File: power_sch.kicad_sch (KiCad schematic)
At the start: 18 parts, among them Q6 RUM002N05T2L, Q7 RUM002N05T2L, U3 TPS7A2601DRVR, U4 TPS7A2601DRVR

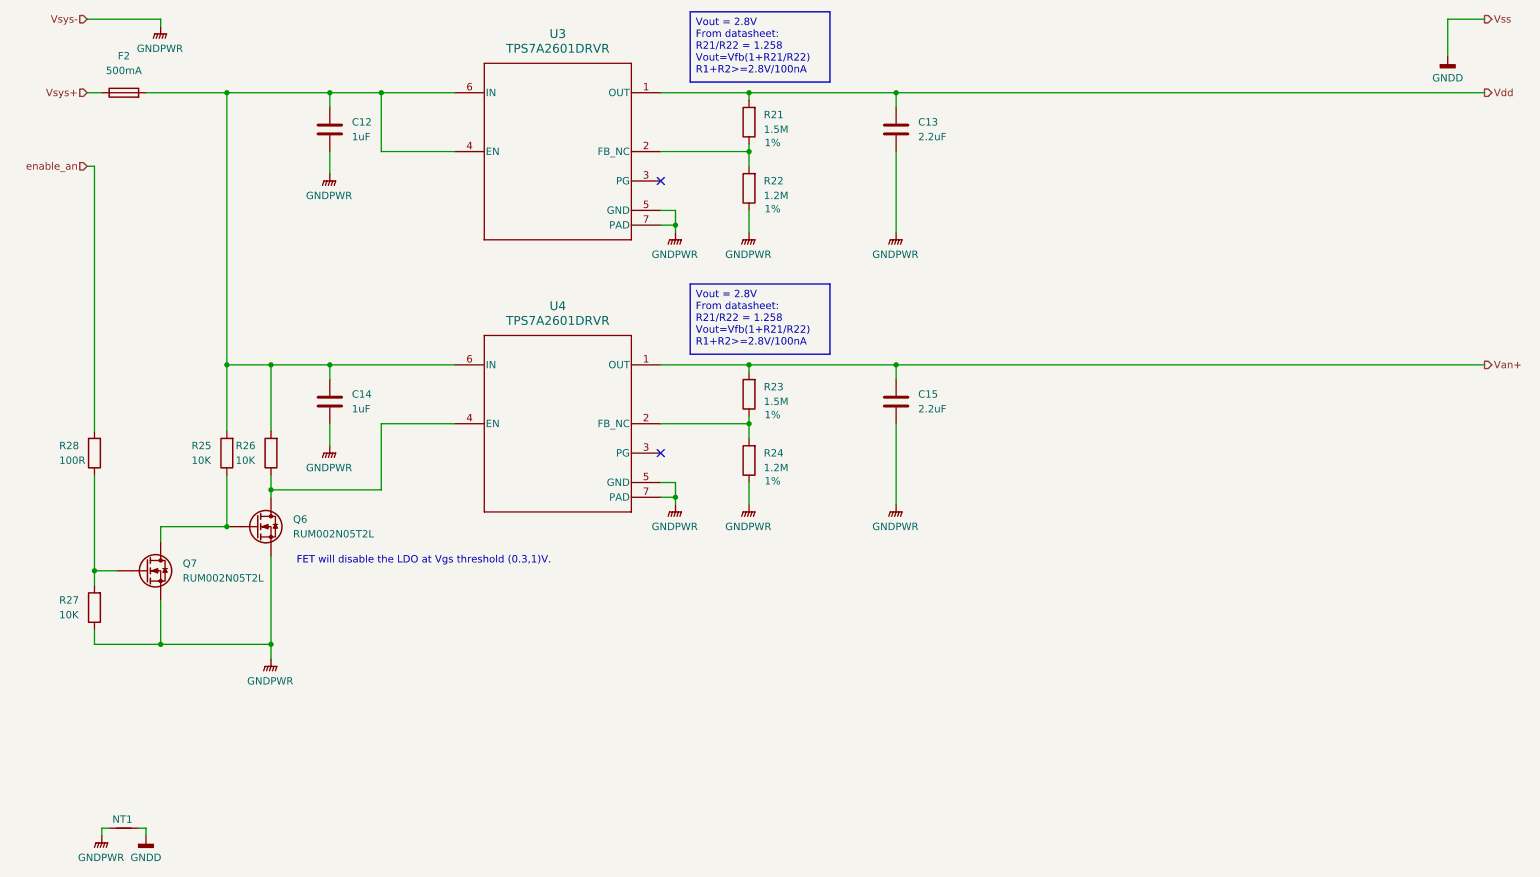
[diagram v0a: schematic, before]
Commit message: Add wiring, change footprint to avoid fatal errors at pads.
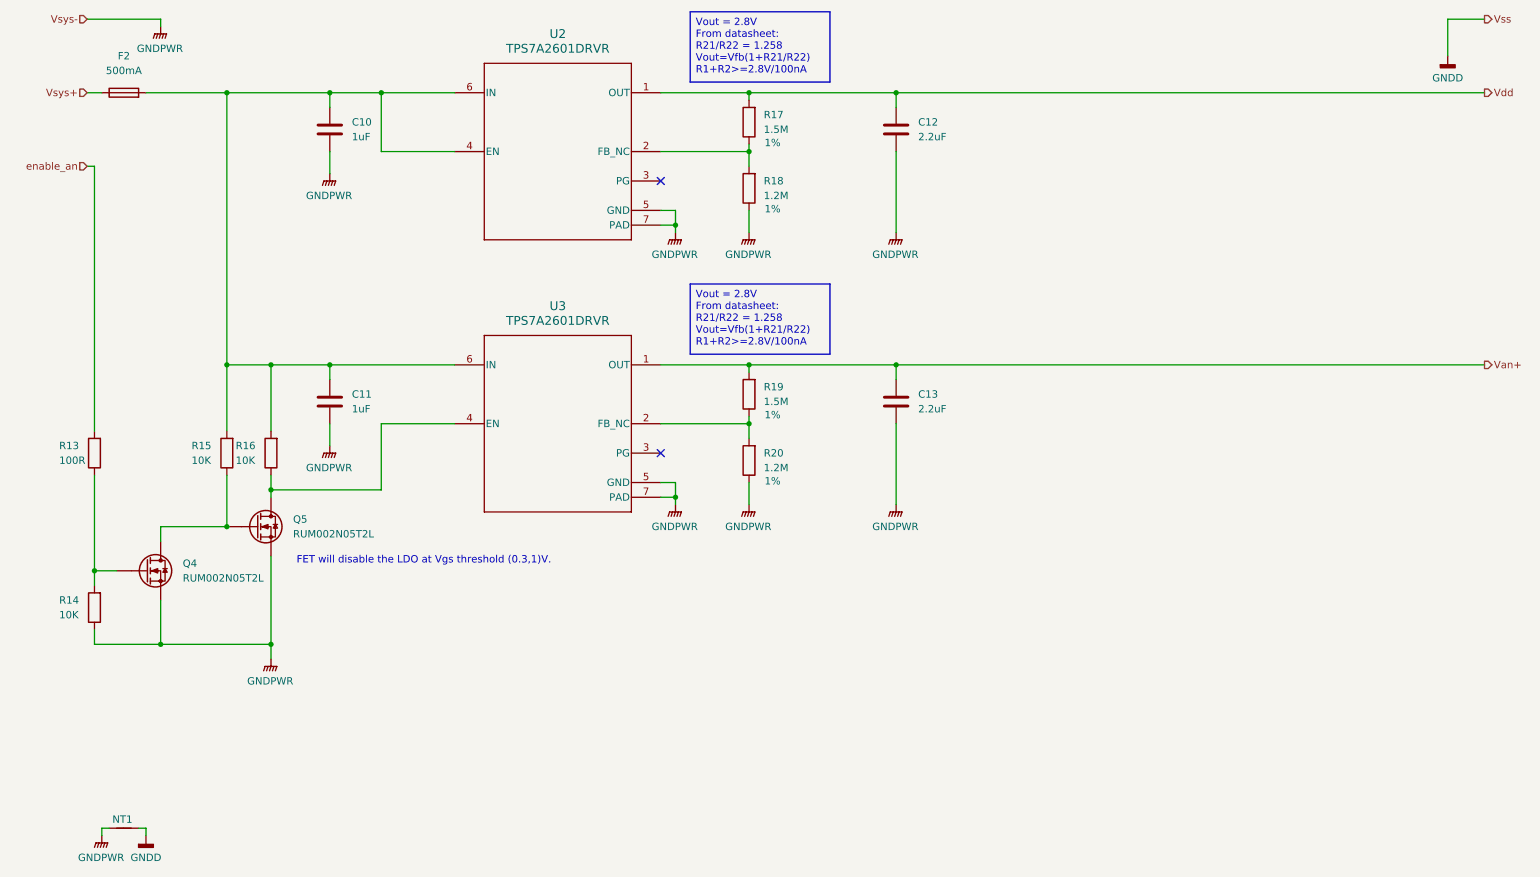
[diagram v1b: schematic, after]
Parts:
- renumbered C12 to C10, C14 to C11, C13 to C12, C15 to C13, Q7 to Q4, Q6 to Q5, R28 to R13, R27 to R14, R25 to R15, R26 to R16, R21 to R17, R22 to R18, R23 to R19, R24 to R20, U3 to U2, U4 to U3
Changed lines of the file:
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@@
 		(dnp no)
 		(fields_autoplaced yes)
-		(property "Reference" "C13"
+		(property "Reference" "C12"
 			(at 168.91 49.5299 0)
 			(show_name no)
@@
 			(project "MoistureESP"
 				(path "/f2b9f638-139e-46ec-aa60-77c4af989196/49685a81-7509-4241-9c59-8f2ca08912fe"
-					(reference "C13")
+					(reference "C12")
 					(unit 1)
 				)
@@
 		(in_pos_files yes)
 		(dnp no)
-		(property "Reference" "R24"
+		(property "Reference" "R20"
 			(at 142.24 106.6799 0)
 			(show_name no)
@@
 			(project "MoistureESP"
 				(path "/f2b9f638-139e-46ec-aa60-77c4af989196/49685a81-7509-4241-9c59-8f2ca08912fe"
-					(reference "R24")
+					(reference "R20")
 					(unit 1)
 				)
@@
 		(in_pos_files yes)
 		(dnp no)
-		(property "Reference" "R23"
+		(property "Reference" "R19"
 			(at 142.24 95.2499 0)
 			(show_name no)
@@
 			(project "MoistureESP"
 				(path "/f2b9f638-139e-46ec-aa60-77c4af989196/49685a81-7509-4241-9c59-8f2ca08912fe"
-					(reference "R23")
+					(reference "R19")
 					(unit 1)
 				)
@@
 		(dnp no)
 		(fields_autoplaced yes)
-		(property "Reference" "#PWR061"
+		(property "Reference" "#PWR031"
 			(at 67.31 63.5 0)
 			(hide yes)
@@
 			(project "MoistureESP"
 				(path "/f2b9f638-139e-46ec-aa60-77c4af989196/49685a81-7509-4241-9c59-8f2ca08912fe"
-					(reference "#PWR061")
+					(reference "#PWR031")
 					(unit 1)
 				)
@@
 		(dnp no)
 		(fields_autoplaced yes)
-		(property "Reference" "#PWR09"
+		(property "Reference" "#PWR028"
 			(at 35.56 179.07 0)
 			(hide yes)
@@
 			(project "MoistureESP"
 				(path "/f2b9f638-139e-46ec-aa60-77c4af989196/49685a81-7509-4241-9c59-8f2ca08912fe"
-					(reference "#PWR09")
+					(reference "#PWR028")
 					(unit 1)
 				)
@@
 		(in_pos_files yes)
 		(dnp no)
-		(property "Reference" "R25"
+		(property "Reference" "R15"
 			(at 43.434 105.41 0)
 			(show_name no)
@@
 			(project "MoistureESP"
 				(path "/f2b9f638-139e-46ec-aa60-77c4af989196/49685a81-7509-4241-9c59-8f2ca08912fe"
-					(reference "R25")
+					(reference "R15")
 					(unit 1)
 				)
@@
 		(dnp no)
 		(fields_autoplaced yes)
-		(property "Reference" "#PWR073"
+		(property "Reference" "#PWR034"
 			(at 127 120.65 0)
 			(hide yes)
@@
 			(project "MoistureESP"
 				(path "/f2b9f638-139e-46ec-aa60-77c4af989196/49685a81-7509-4241-9c59-8f2ca08912fe"
-					(reference "#PWR073")
+					(reference "#PWR034")
 					(unit 1)
 				)
@@
 		(dnp no)
 		(fields_autoplaced yes)
-		(property "Reference" "U3"
+		(property "Reference" "U2"
 			(at 106.68 34.29 0)
 			(show_name no)
@@
 			(project "MoistureESP"
 				(path "/f2b9f638-139e-46ec-aa60-77c4af989196/49685a81-7509-4241-9c59-8f2ca08912fe"
-					(reference "U3")
+					(reference "U2")
 					(unit 1)
 				)
@@
 		(dnp no)
 		(fields_autoplaced yes)
-		(property "Reference" "#PWR068"
+		(property "Reference" "#PWR033"
 			(at 127 73.66 0)
 			(hide yes)
@@
 			(project "MoistureESP"
 				(path "/f2b9f638-139e-46ec-aa60-77c4af989196/49685a81-7509-4241-9c59-8f2ca08912fe"
-					(reference "#PWR068")
+					(reference "#PWR033")
 					(unit 1)
 				)
@@
 		(dnp no)
 		(fields_autoplaced yes)
-		(property "Reference" "#PWR018"
+		(property "Reference" "#PWR039"
 			(at 260.35 44.45 0)
 			(hide yes)
@@
 			(project "MoistureESP"
 				(path "/f2b9f638-139e-46ec-aa60-77c4af989196/49685a81-7509-4241-9c59-8f2ca08912fe"
-					(reference "#PWR018")
+					(reference "#PWR039")
 					(unit 1)
 				)
@@
 		(dnp no)
 		(fields_autoplaced yes)
-		(property "Reference" "#PWR076"
+		(property "Reference" "#PWR032"
 			(at 67.31 110.49 0)
 			(hide yes)
@@
 			(project "MoistureESP"
 				(path "/f2b9f638-139e-46ec-aa60-77c4af989196/49685a81-7509-4241-9c59-8f2ca08912fe"
-					(reference "#PWR076")
+					(reference "#PWR032")
 					(unit 1)
 				)
@@
 		(in_pos_files yes)
 		(dnp no)
-		(property "Reference" "R21"
+		(property "Reference" "R17"
 			(at 142.24 48.2599 0)
 			(show_name no)
@@
 			(project "MoistureESP"
 				(path "/f2b9f638-139e-46ec-aa60-77c4af989196/49685a81-7509-4241-9c59-8f2ca08912fe"
-					(reference "R21")
+					(reference "R17")
 					(unit 1)
 				)
@@
 		(dnp no)
 		(fields_autoplaced yes)
-		(property "Reference" "Q6"
+		(property "Reference" "Q5"
 			(at 60.96 118.1099 0)
 			(show_name no)
@@
 			(project "MoistureESP"
 				(path "/f2b9f638-139e-46ec-aa60-77c4af989196/49685a81-7509-4241-9c59-8f2ca08912fe"
-					(reference "Q6")
+					(reference "Q5")
 					(unit 1)
 				)
@@
 		(dnp no)
 		(fields_autoplaced yes)
-		(property "Reference" "C14"
+		(property "Reference" "C11"
 			(at 71.12 96.5199 0)
 			(show_name no)
@@
 			(project "MoistureESP"
 				(path "/f2b9f638-139e-46ec-aa60-77c4af989196/49685a81-7509-4241-9c59-8f2ca08912fe"
-					(reference "C14")
+					(reference "C11")
 					(unit 1)
 				)
@@
 		(dnp no)
 		(fields_autoplaced yes)
-		(property "Reference" "Q7"
+		(property "Reference" "Q4"
 			(at 41.91 125.7299 0)
 			(show_name no)
@@
 			(project "MoistureESP"
 				(path "/f2b9f638-139e-46ec-aa60-77c4af989196/49685a81-7509-4241-9c59-8f2ca08912fe"
-					(reference "Q7")
+					(reference "Q4")
 					(unit 1)
 				)
@@
 		(dnp no)
 		(fields_autoplaced yes)
-		(property "Reference" "#PWR077"
+		(property "Reference" "#PWR030"
 			(at 57.15 147.32 0)
 			(hide yes)
@@
 			(project "MoistureESP"
 				(path "/f2b9f638-139e-46ec-aa60-77c4af989196/49685a81-7509-4241-9c59-8f2ca08912fe"
-					(reference "#PWR077")
+					(reference "#PWR030")
 					(unit 1)
 				)
@@
 		(dnp no)
 		(fields_autoplaced yes)
-		(property "Reference" "#PWR074"
+		(property "Reference" "#PWR036"
 			(at 139.7 120.65 0)
 			(hide yes)
@@
 			(project "MoistureESP"
 				(path "/f2b9f638-139e-46ec-aa60-77c4af989196/49685a81-7509-4241-9c59-8f2ca08912fe"
-					(reference "#PWR074")
+					(reference "#PWR036")
 					(unit 1)
 				)
@@
 		(dnp no)
 		(fields_autoplaced yes)
-		(property "Reference" "#PWR08"
+		(property "Reference" "#PWR027"
 			(at 27.94 177.8 0)
 			(hide yes)
@@
 			(project "MoistureESP"
 				(path "/f2b9f638-139e-46ec-aa60-77c4af989196/49685a81-7509-4241-9c59-8f2ca08912fe"
-					(reference "#PWR08")
+					(reference "#PWR027")
 					(unit 1)
 				)
@@
 		(dnp no)
 		(fields_autoplaced yes)
-		(property "Reference" "C12"
+		(property "Reference" "C10"
 			(at 71.12 49.5299 0)
 			(show_name no)
@@
 			(project "MoistureESP"
 				(path "/f2b9f638-139e-46ec-aa60-77c4af989196/49685a81-7509-4241-9c59-8f2ca08912fe"
-					(reference "C12")
+					(reference "C10")
 					(unit 1)
 				)
@@
 		(in_pos_files yes)
 		(dnp no)
-		(property "Reference" "R22"
+		(property "Reference" "R18"
 			(at 142.24 59.6899 0)
 			(show_name no)
@@
 			(project "MoistureESP"
 				(path "/f2b9f638-139e-46ec-aa60-77c4af989196/49685a81-7509-4241-9c59-8f2ca08912fe"
-					(reference "R22")
+					(reference "R18")
 					(unit 1)
 				)
@@
 		(in_pos_files yes)
 		(dnp no)
-		(property "Reference" "R28"
+		(property "Reference" "R13"
 			(at 20.574 105.41 0)
 			(show_name no)
@@
 			(project "MoistureESP"
 				(path "/f2b9f638-139e-46ec-aa60-77c4af989196/49685a81-7509-4241-9c59-8f2ca08912fe"
-					(reference "R28")
+					(reference "R13")
 					(unit 1)
 				)
@@
 		(in_pos_files yes)
 		(dnp no)
-		(property "Reference" "R27"
+		(property "Reference" "R14"
 			(at 20.574 132.08 0)
 			(show_name no)
@@
 			(project "MoistureESP"
 				(path "/f2b9f638-139e-46ec-aa60-77c4af989196/49685a81-7509-4241-9c59-8f2ca08912fe"
-					(reference "R27")
+					(reference "R14")
 					(unit 1)
 				)
@@
 		(dnp no)
 		(fields_autoplaced yes)
-		(property "Reference" "C15"
+		(property "Reference" "C13"
 			(at 168.91 96.5199 0)
 			(show_name no)
@@
 			(project "MoistureESP"
 				(path "/f2b9f638-139e-46ec-aa60-77c4af989196/49685a81-7509-4241-9c59-8f2ca08912fe"
-					(reference "C15")
+					(reference "C13")
 					(unit 1)
 				)
@@
 		(dnp no)
 		(fields_autoplaced yes)
-		(property "Reference" "#PWR075"
+		(property "Reference" "#PWR038"
 			(at 165.1 120.65 0)
 			(hide yes)
@@
 			(project "MoistureESP"
 				(path "/f2b9f638-139e-46ec-aa60-77c4af989196/49685a81-7509-4241-9c59-8f2ca08912fe"
-					(reference "#PWR075")
+					(reference "#PWR038")
 					(unit 1)
 				)
@@
 		(dnp no)
 		(fields_autoplaced yes)
-		(property "Reference" "#PWR071"
+		(property "Reference" "#PWR035"
 			(at 139.7 73.66 0)
 			(hide yes)
@@
 			(project "MoistureESP"
 				(path "/f2b9f638-139e-46ec-aa60-77c4af989196/49685a81-7509-4241-9c59-8f2ca08912fe"
-					(reference "#PWR071")
+					(reference "#PWR035")
 					(unit 1)
 				)
@@
 		(dnp no)
 		(fields_autoplaced yes)
-		(property "Reference" "#PWR072"
+		(property "Reference" "#PWR037"
 			(at 165.1 73.66 0)
 			(hide yes)
@@
 			(project "MoistureESP"
 				(path "/f2b9f638-139e-46ec-aa60-77c4af989196/49685a81-7509-4241-9c59-8f2ca08912fe"
-					(reference "#PWR072")
+					(reference "#PWR037")
 					(unit 1)
 				)
@@
 		(dnp no)
 		(fields_autoplaced yes)
-		(property "Reference" "U4"
+		(property "Reference" "U3"
 			(at 106.68 81.28 0)
 			(show_name no)
@@
 			(project "MoistureESP"
 				(path "/f2b9f638-139e-46ec-aa60-77c4af989196/49685a81-7509-4241-9c59-8f2ca08912fe"
-					(reference "U4")
+					(reference "U3")
 					(unit 1)
 				)
@@
 		(in_pos_files yes)
 		(dnp no)
-		(property "Reference" "R26"
+		(property "Reference" "R16"
 			(at 51.054 105.41 0)
 			(show_name no)
@@
 			(project "MoistureESP"
 				(path "/f2b9f638-139e-46ec-aa60-77c4af989196/49685a81-7509-4241-9c59-8f2ca08912fe"
-					(reference "R26")
-					(unit 1)
-				)
+					(reference "R16")
+					(unit 1)
+				)

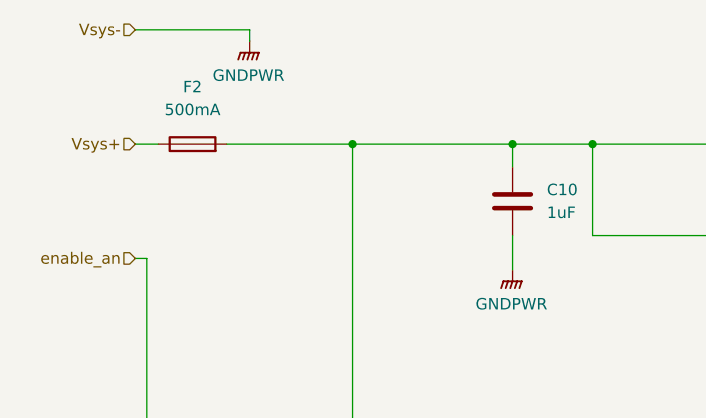
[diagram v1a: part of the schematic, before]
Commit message: Refine VBAT zone and add wiring under MCU.
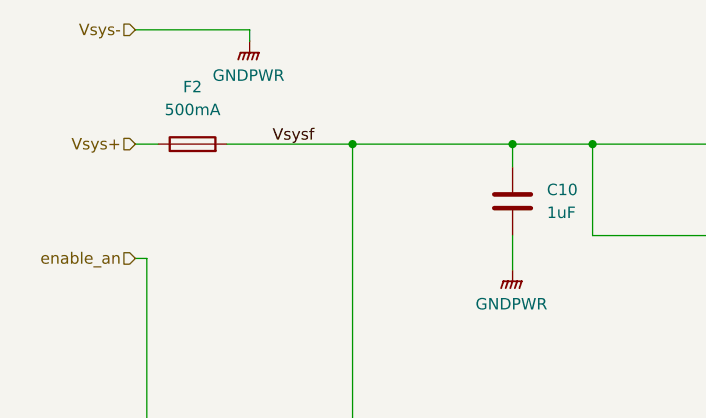
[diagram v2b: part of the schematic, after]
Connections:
- net Vsysf: now reaches C10.2, C11.2, F2.2, R15.2, R16.2, U2.4 (EN), U2.6 (IN), U3.6 (IN)
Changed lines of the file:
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@@
+		)
+	)
+	(label "Vsysf"
+		(at 40.64 44.45 0)
+		(effects
+			(font
+				(size 1.27 1.27)
+			)
+			(justify left bottom)
 		)
 	)

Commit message: Fixing DRCs. Modify polygons.
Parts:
- NT1: footprint (none) -> NetTie:NetTie-2_SMD_Pad2.0mm
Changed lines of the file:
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@@
 			)
 		)
-		(property "Footprint" ""
+		(property "Footprint" "NetTie:NetTie-2_SMD_Pad2.0mm"
 			(at 31.75 171.45 0)
 			(hide yes)

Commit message: Export BOM, change page headers.
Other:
- company: (none) -> B.Major
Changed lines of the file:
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@@
 	(generator_version "10.0")
 	(paper "A4")
+	(title_block
+		(date "2026-03-27")
+		(rev "1")
+		(company "B.Major")
+	)
 	(text "FET will disable the LDO at Vgs threshold (0.3,1)V."
 		(exclude_from_sim no)
